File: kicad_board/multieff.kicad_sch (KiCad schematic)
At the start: 26 parts

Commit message: Latest pcb version
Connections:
- net 5V: now also Pisound1.2 (Pin_2); no longer Pisound1.1 (Pin_1)
- net GND: now also Pisound1.1 (Pin_1); no longer Pisound1.2 (Pin_2)
- net SCL: now also ADC1.3 (Pin_3), Pisound1.14 (Pin_14); no longer ADC1.4 (Pin_4), Pisound1.13 (Pin_13)
- net SDA: now also ADC1.4 (Pin_4), Pisound1.13 (Pin_13); no longer ADC1.3 (Pin_3), Pisound1.14 (Pin_14)
- net at MCP1R1.11 (Pin_11): now also RE1.4 (Pin_4); no longer RE1.5 (Pin_5)
- net at MCP1R1.12 (Pin_12): now also Joystick1.1 (Pin_1); no longer RE2.3 (Pin_3)
- net at MCP1R1.13 (Pin_13): now also RE1.3 (Pin_3); no longer RE1.4 (Pin_4)
- net at MCP1R1.14 (Pin_14): now also RE2.3 (Pin_3); no longer RE2.4 (Pin_4)
- net at MCP1R1.15 (Pin_15): now also RE2.5 (Pin_5); no longer RE1.3 (Pin_3)
- net at MCP1R1.16 (Pin_16): now also RE2.4 (Pin_4); no longer RE2.5 (Pin_5)
- net at MCP1R1.20 (Pin_20): no longer Joystick1.4 (Pin_4)
- net at MCP1R1.9 (Pin_9): now also RE1.5 (Pin_5)
- net +3.3V: now reaches Pisound1.4 (Pin_4)
- net +3.3V: now also ADC1.1 (Pin_1), Joystick1.4 (Pin_4), MCD1L1.1 (Pin_1), MCP2L1.1 (Pin_1), MCP2L1.8 (Pin_8), RE1.2 (Pin_2), RE2.2 (Pin_2), RE3.2 (Pin_2), RE4.2 (Pin_2)
- removed net 3.3V: ADC1.1 (Pin_1), Joystick1.1 (Pin_1), MCD1L1.1 (Pin_1), MCP2L1.1 (Pin_1), MCP2L1.8 (Pin_8), Pisound1.3 (Pin_3), RE1.2 (Pin_2), RE2.2 (Pin_2), RE3.2 (Pin_2), RE4.2 (Pin_2)

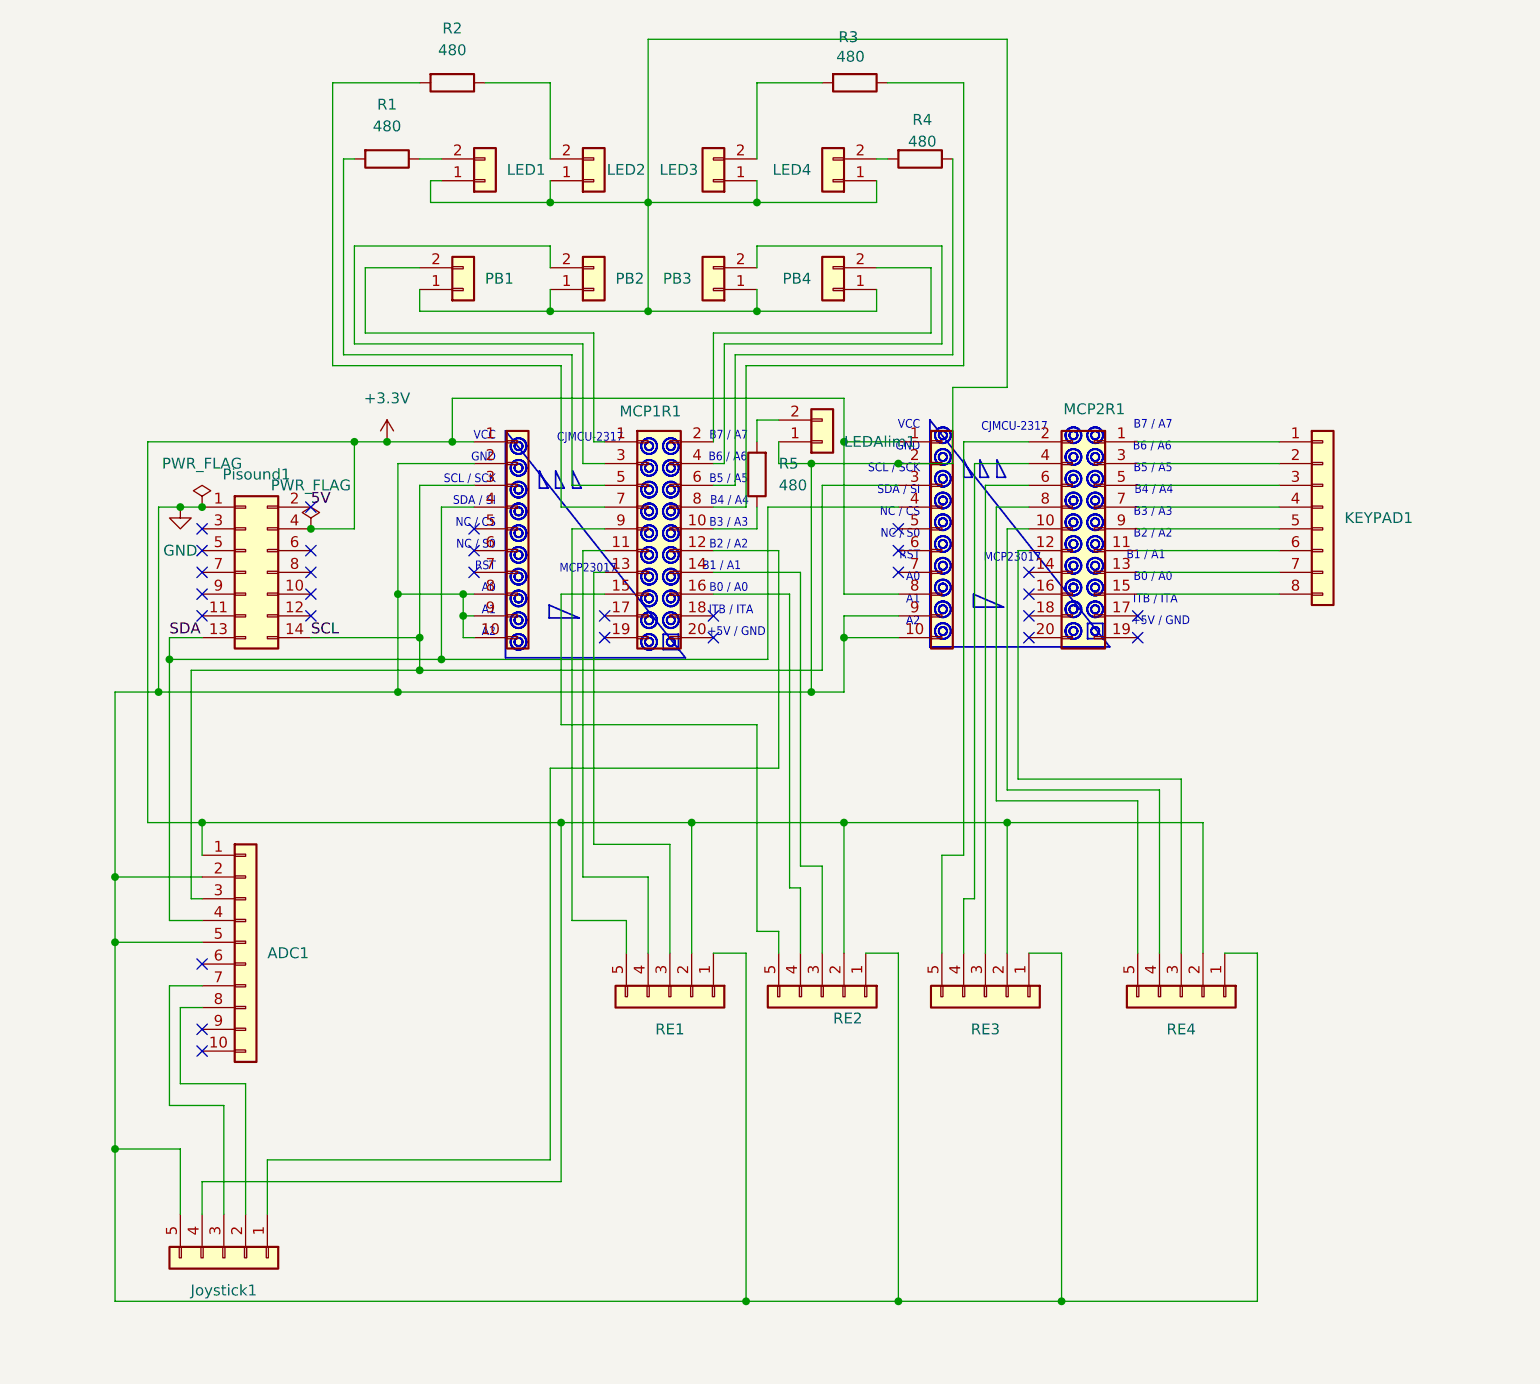
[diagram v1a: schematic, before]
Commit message: Add connector for expression pedal
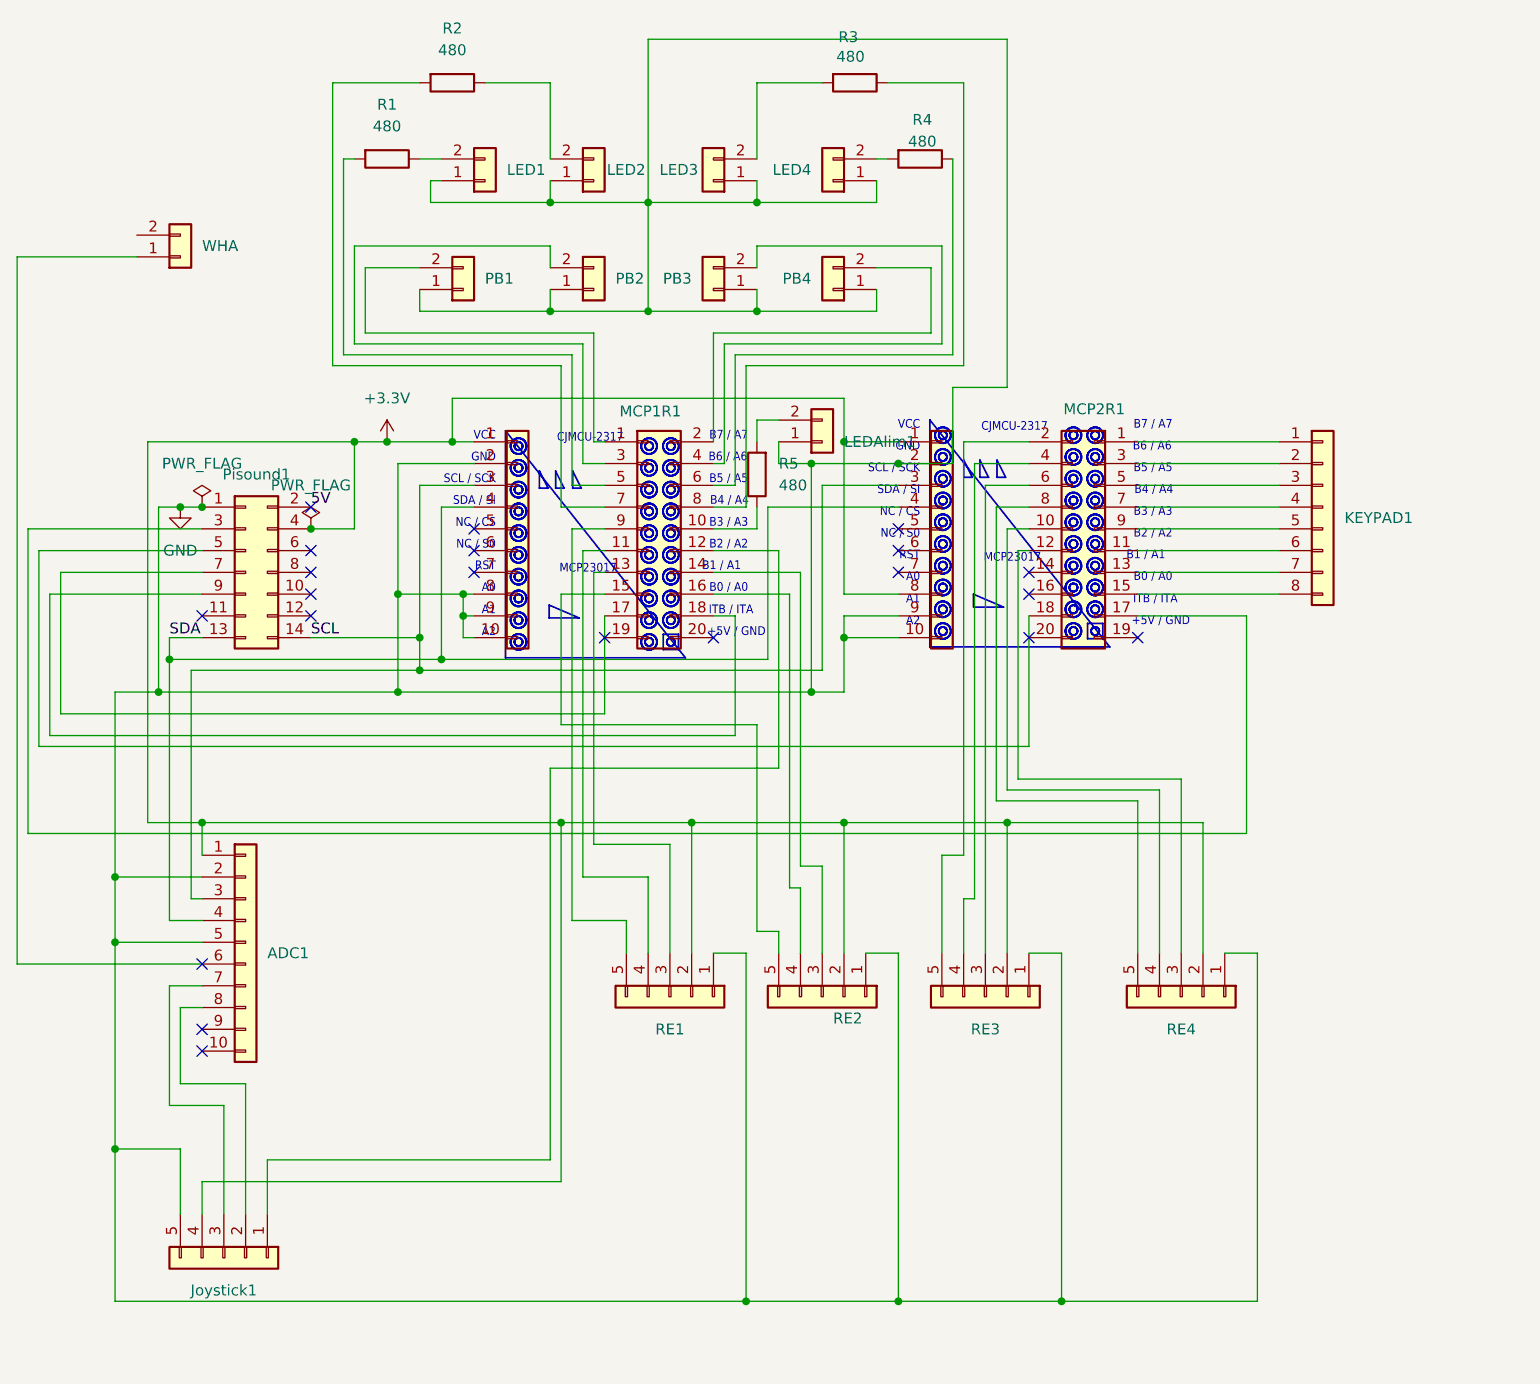
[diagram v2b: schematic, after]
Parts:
- added WHA: Conn_01x02, Connector_Wire:SolderWire-0.1sqmm_1x02_P3.6mm_D0.4mm_OD1mm, symbol Connector_Generic:Conn_01x02
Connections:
- net at MCP1R1.17 (Pin_17): now also Pisound1.7 (Pin_7)
- net at MCP1R1.18 (Pin_18): now also Pisound1.9 (Pin_9)
- net at ADC1.6 (Pin_6): now also WHA.1 (Pin_1)
- net at Pisound1.3 (Pin_3): now also MCP2R1.17 (Pin_17)
- net at Pisound1.5 (Pin_5): now also MCP2R1.18 (Pin_18)
- no-connect marks 29 -> 21

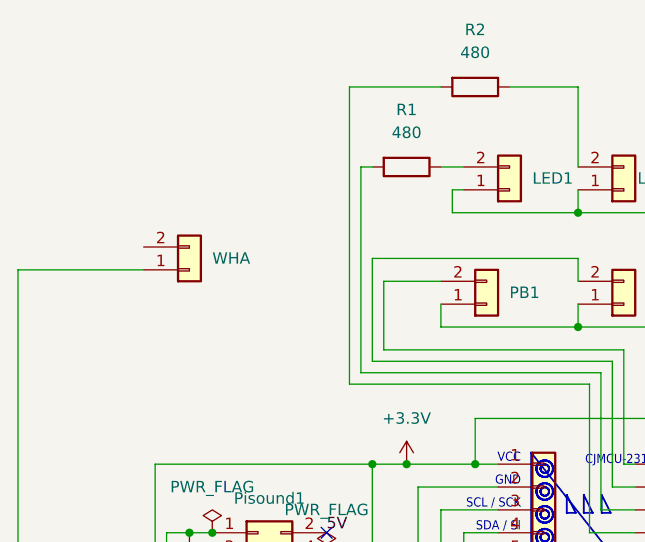
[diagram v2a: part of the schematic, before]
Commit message: Add component numbering
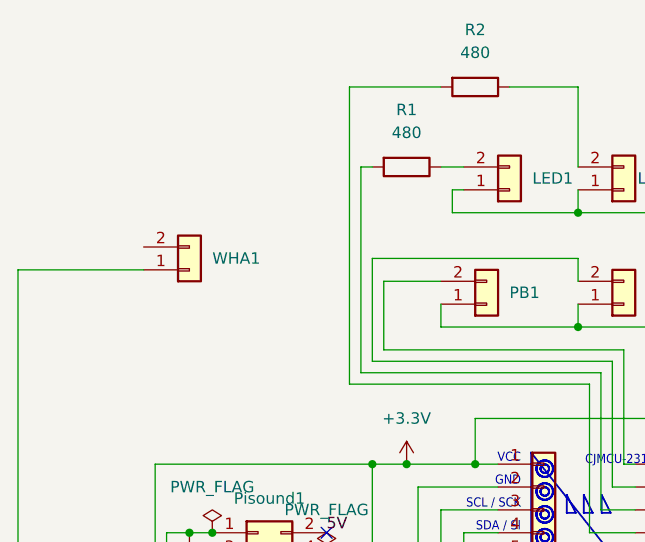
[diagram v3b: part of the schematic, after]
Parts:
- renumbered WHA to WHA1
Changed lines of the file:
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@@
 		(on_board yes)
 		(dnp no)
-		(property "Reference" "WHA"
+		(property "Reference" "WHA1"
 			(at 35.56 41.9101 0)
 			(effects
@@
 			(project "multieff"
 				(path "/01a67eee-3893-4e68-bed0-a04a64951ab4"
-					(reference "WHA")
+					(reference "WHA1")
 					(unit 1)
 				)

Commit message: With zones and jst connectors
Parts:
- removed WHA1: Conn_01x02, Connector_Wire:SolderWire-0.1sqmm_1x02_P3.6mm_D0.4mm_OD1mm, symbol Connector_Generic:Conn_01x02
- added C1: C, Capacitor_THT:C_Disc_D5.0mm_W2.5mm_P2.50mm, symbol Device:C
- added C2: C_Polarized, Capacitor_THT:CP_Radial_D5.0mm_P2.00mm, symbol Device:C_Polarized
- added H1, H2, H3, H4: MountingHole, MountingHole:MountingHole_3.2mm_M3, symbol Mechanical:MountingHole
- added J1: Wha1, Connector_JST:JST_XH_B3B-XH-AM_1x03_P2.50mm_Vertical, symbol Connector_Generic:Conn_01x03
- Joystick1, RE1, RE2, RE3, RE4: footprint Connector_Wire:SolderWire-0.1sqmm_1x05_P3.6mm_D0.4mm_OD1mm -> Connector_JST:JST_XH_B5B-XH-AM_1x05_P2.50mm_Vertical
- LED1, LED2, LED3, LED4, LEDAlim1, PB1, PB2, PB3, PB4: footprint Connector_Wire:SolderWire-0.1sqmm_1x02_P3.6mm_D0.4mm_OD1mm -> Connector_JST:JST_XH_B2B-XH-AM_1x02_P2.50mm_Vertical
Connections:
- net +3.3V: now also R5.2, C1.1, C2.1, J1.2 (Pin_2)
- net GND: now also C1.2, C2.2, J1.1 (Pin_1)
- net at MCP1R1.10 (Pin_10): no longer R5.1
- net at LEDAlim1.2 (Pin_2): now also R5.1; no longer R5.2
- net at ADC1.6 (Pin_6): now also J1.3 (Pin_3)
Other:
- moved on the sheet: R5

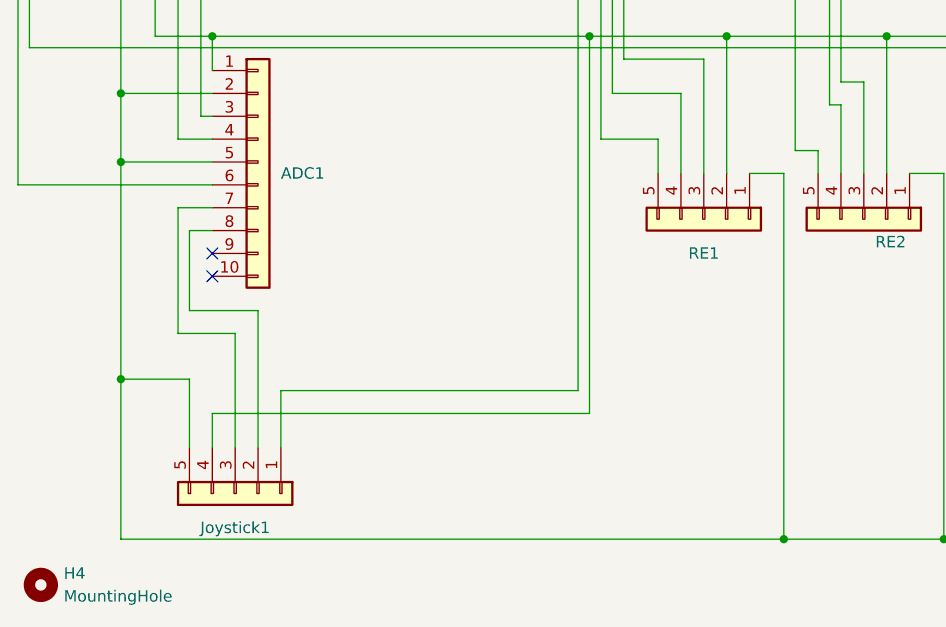
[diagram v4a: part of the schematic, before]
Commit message: Correct joystick jst orientation
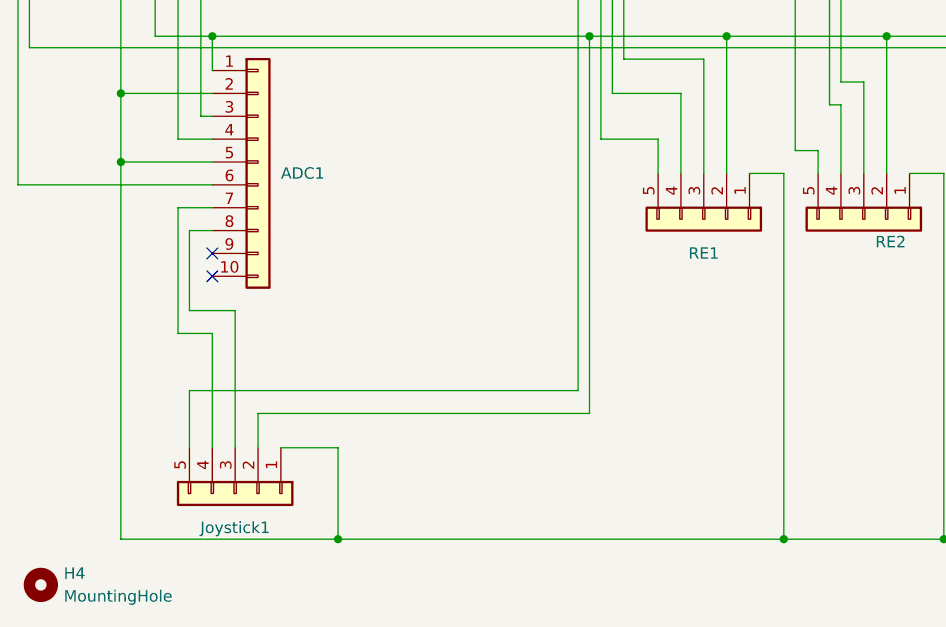
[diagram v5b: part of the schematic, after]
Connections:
- net +3.3V: now also Joystick1.2 (Pin_2); no longer Joystick1.4 (Pin_4)
- net GND: now also Joystick1.1 (Pin_1); no longer Joystick1.5 (Pin_5)
- net at MCP1R1.12 (Pin_12): now also Joystick1.5 (Pin_5); no longer Joystick1.1 (Pin_1)
- net at ADC1.7 (Pin_7): now also Joystick1.4 (Pin_4); no longer Joystick1.3 (Pin_3)
- net at ADC1.8 (Pin_8): now also Joystick1.3 (Pin_3); no longer Joystick1.2 (Pin_2)
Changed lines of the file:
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@@
+	)
+	(junction
+		(at 49.53 165.1)
+		(diameter 0)
+		(color 0 0 0 0)
 	)
 	(junction
@@
 	(junction
 		(at 58.42 93.98)
-		(diameter 0)
-		(color 0 0 0 0)
-	)
-	(junction
-		(at 25.4 147.32)
 		(diameter 0)
 		(color 0 0 0 0)
@@
 	(wire
 		(pts
+			(xy 49.53 154.94) (xy 49.53 165.1)
+		)
+		(stroke
+			(width 0)
+			(type default)
+		)
+	)
+	(wire
+		(pts
 			(xy 81.28 80.01) (xy 81.28 111.76)
 		)
@@
 	(wire
 		(pts
-			(xy 38.1 154.94) (xy 38.1 142.24)
-		)
-		(stroke
-			(width 0)
-			(type default)
-		)
-	)
-	(wire
-		(pts
 			(xy 67.31 82.55) (xy 66.04 82.55)
 		)
@@
 	(wire
 		(pts
+			(xy 38.1 154.94) (xy 38.1 139.7)
+		)
+		(stroke
+			(width 0)
+			(type default)
+		)
+	)
+	(wire
+		(pts
 			(xy 132.08 124.46) (xy 135.89 124.46)
 		)
@@
 	(wire
 		(pts
+			(xy 35.56 154.94) (xy 35.56 142.24)
+		)
+		(stroke
+			(width 0)
+			(type default)
+		)
+	)
+	(wire
+		(pts
 			(xy 60.96 91.44) (xy 107.95 91.44)
 		)
@@
 	(wire
 		(pts
+			(xy 33.02 148.59) (xy 33.02 154.94)
+		)
+		(stroke
+			(width 0)
+			(type default)
+		)
+	)
+	(wire
+		(pts
 			(xy 124.46 118.11) (xy 124.46 124.46)
 		)
@@
 	(wire
 		(pts
+			(xy 40.64 151.13) (xy 77.47 151.13)
+		)
+		(stroke
+			(width 0)
+			(type default)
+		)
+	)
+	(wire
+		(pts
 			(xy 102.87 67.31) (xy 102.87 64.77)
 		)
@@
 	(wire
 		(pts
-			(xy 40.64 139.7) (xy 33.02 139.7)
+			(xy 33.02 139.7) (xy 38.1 139.7)
 		)
 		(stroke
@@
 	(wire
 		(pts
+			(xy 33.02 148.59) (xy 76.2 148.59)
+		)
+		(stroke
+			(width 0)
+			(type default)
+		)
+	)
+	(wire
+		(pts
 			(xy 30.48 81.28) (xy 24.13 81.28)
 		)
@@
 	(wire
 		(pts
-			(xy 43.18 148.59) (xy 43.18 154.94)
-		)
-		(stroke
-			(width 0)
-			(type default)
-		)
-	)
-	(wire
-		(pts
 			(xy 105.41 114.3) (xy 107.95 114.3)
 		)
@@
 	(wire
 		(pts
+			(xy 40.64 154.94) (xy 40.64 151.13)
+		)
+		(stroke
+			(width 0)
+			(type default)
+		)
+	)
+	(wire
+		(pts
 			(xy 66.04 82.55) (xy 58.42 82.55)
 		)
@@
 	(wire
 		(pts
-			(xy 25.4 165.1) (xy 25.4 147.32)
-		)
-		(stroke
-			(width 0)
-			(type default)
-		)
-	)
-	(wire
-		(pts
 			(xy 35.56 87.63) (xy 31.75 87.63)
 		)
@@
 	(wire
 		(pts
-			(xy 38.1 142.24) (xy 31.75 142.24)
+			(xy 31.75 142.24) (xy 35.56 142.24)
 		)
 		(stroke
@@
 	(wire
 		(pts
-			(xy 25.4 147.32) (xy 33.02 147.32)
-		)
-		(stroke
-			(width 0)
-			(type default)
-		)
-	)
-	(wire
-		(pts
 			(xy 144.78 85.09) (xy 157.48 85.09)
 		)
@@
 	(wire
 		(pts
-			(xy 35.56 151.13) (xy 77.47 151.13)
-		)
-		(stroke
-			(width 0)
-			(type default)
-		)
-	)
-	(wire
-		(pts
 			(xy 124.46 22.86) (xy 124.46 55.88)
 		)
@@
 	(wire
 		(pts
-			(xy 76.2 148.59) (xy 43.18 148.59)
-		)
-		(stroke
-			(width 0)
-			(type default)
-		)
-	)
-	(wire
-		(pts
 			(xy 53.34 53.34) (xy 53.34 41.91)
 		)
@@
 	(wire
 		(pts
-			(xy 25.4 123.19) (xy 25.4 147.32)
+			(xy 25.4 123.19) (xy 25.4 165.1)
 		)
 		(stroke
@@
 		)
 	)
-	(wire
-		(pts
-			(xy 40.64 154.94) (xy 40.64 139.7)
-		)
-		(stroke
-			(width 0)
-			(type default)
-		)
-	)
 	(polyline
 		(pts
@@
 	(wire
 		(pts
-			(xy 33.02 154.94) (xy 33.02 147.32)
-		)
-		(stroke
-			(width 0)
-			(type default)
-		)
-	)
-	(wire
-		(pts
 			(xy 121.92 53.34) (xy 121.92 41.91)
 		)
@@
 	(wire
 		(pts
-			(xy 25.4 165.1) (xy 99.06 165.1)
+			(xy 49.53 165.1) (xy 99.06 165.1)
+		)
+		(stroke
+			(width 0)
+			(type default)
+		)
+	)
+	(wire
+		(pts
+			(xy 25.4 165.1) (xy 49.53 165.1)
 		)
 		(stroke
@@
 	(wire
 		(pts
+			(xy 43.18 154.94) (xy 49.53 154.94)
+		)
+		(stroke
+			(width 0)
+			(type default)
+		)
+	)
+	(wire
+		(pts
 			(xy 76.2 102.87) (xy 102.87 102.87)
 		)
@@
 		)
 		(stroke
-			(width 0)
-			(type default)
-		)
-	)
-	(wire
-		(pts
-			(xy 35.56 151.13) (xy 35.56 154.94)
-		)
-		(stroke
